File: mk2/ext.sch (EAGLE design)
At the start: 3 parts

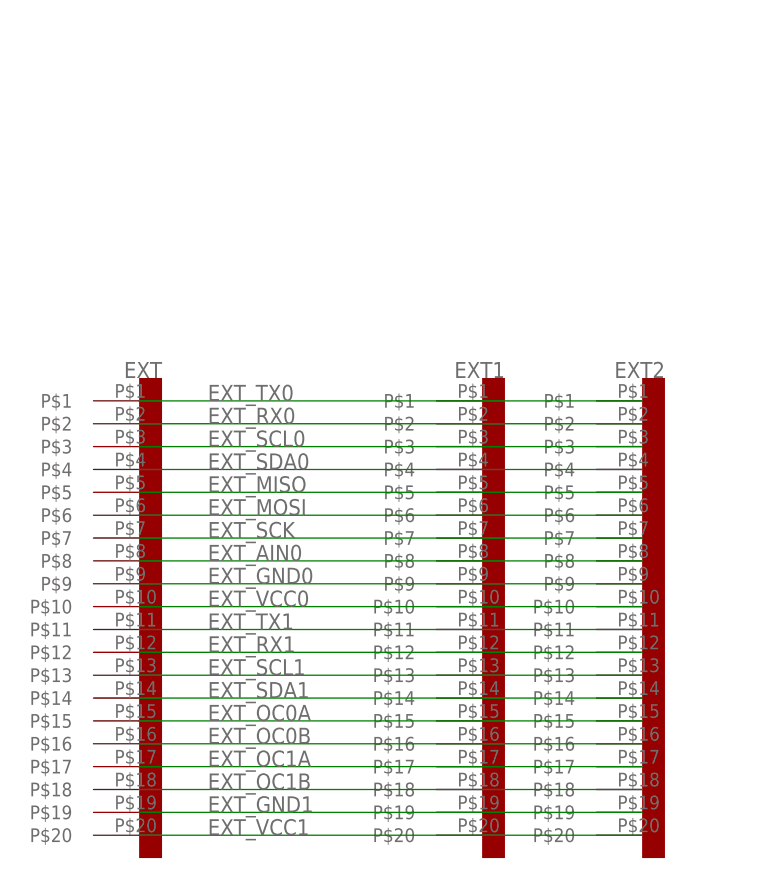
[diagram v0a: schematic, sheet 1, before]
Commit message: [mk2 extension uart]
	- add a uart header and tx/rx config header to the mk2.1 extension
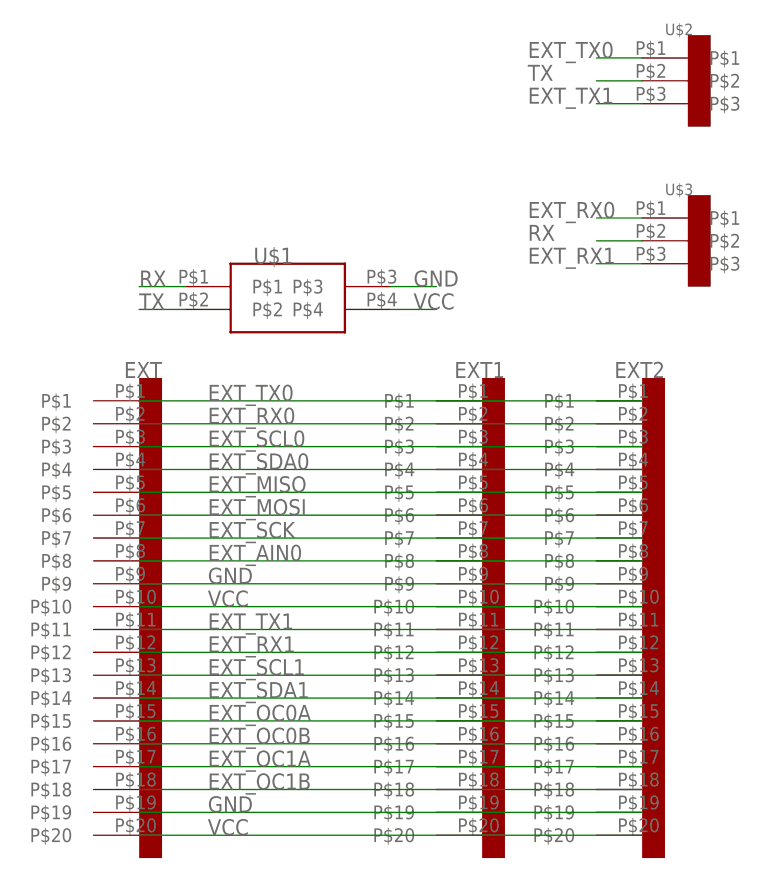
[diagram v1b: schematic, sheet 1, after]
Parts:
- added U$1: CON_DIL_2X2, connector:CON_DIL_2X2
- added U$2, U$3: CON_DIL_3, connector:CON_DIL_3
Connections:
- removed net EXT_GND0: EXT.P$9, EXT1.P$9, EXT2.P$9
- removed net EXT_GND1: EXT.P$19, EXT1.P$19, EXT2.P$19
- removed net EXT_VCC0: EXT.P$10, EXT1.P$10, EXT2.P$10
- removed net EXT_VCC1: EXT.P$20, EXT1.P$20, EXT2.P$20
- new net GND: EXT.P$19, EXT.P$9, EXT1.P$19, EXT1.P$9, EXT2.P$19, EXT2.P$9, U$1.P$3
- new net RX: U$1.P$1, U$3.P$2
- new net TX: U$1.P$2, U$2.P$2
- new net VCC: EXT.P$10, EXT.P$20, EXT1.P$10, EXT1.P$20, EXT2.P$10, EXT2.P$20, U$1.P$4
- net EXT_RX0: now also U$3.P$1
- net EXT_RX1: now also U$3.P$3
- net EXT_TX0: now also U$2.P$1
- net EXT_TX1: now also U$2.P$3
